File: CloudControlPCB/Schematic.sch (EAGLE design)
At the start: 29 parts, among them J1 AUDIO_JACK_TRRSSMD_RA, U1 LPC4088FBD208, U2 SGTL5000XNLA3R2, U3 LD1117S33CTR, X1 PHB_1MM27_2X05_SNT

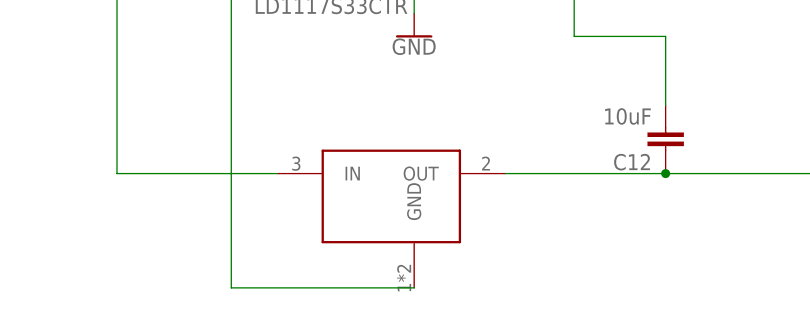
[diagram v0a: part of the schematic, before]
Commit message: Fixed 1.8V regulator connections
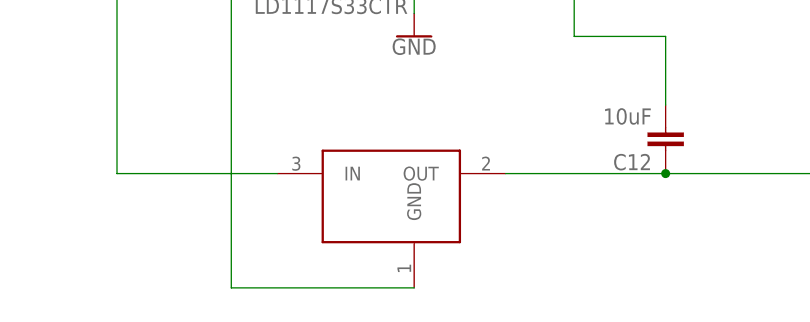
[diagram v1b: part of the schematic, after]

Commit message: finished routing
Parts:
- added C15: 0.1uF, SparkFun-Capacitors:0.1UF-0603-25V-(+80/-20%)
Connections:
- net GND: now also C15.2
- net VCC: now also C15.1
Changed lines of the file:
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@@
 <part name="U3" library="LD1117S33CTR" deviceset="LD1117S33CTR" device=""/>
 <part name="U$1" library="SOT230P700X180-4N" deviceset="SOT230P700X180-4N" device=""/>
+<part name="C15" library="SparkFun-Capacitors" deviceset="0.1UF" device="-0603-25V-(+80/-20%)" value="0.1uF"/>
 </parts>
 <sheets>
@@
 </instance>
 <instance part="U$1" gate="G$1" x="-104.14" y="-101.6" smashed="yes"/>
+<instance part="C15" gate="G$1" x="-116.84" y="-104.14" smashed="yes">
+<attribute name="NAME" x="-115.316" y="-101.219" size="1.778" layer="95" font="vector"/>
+<attribute name="VALUE" x="-115.316" y="-106.299" size="1.778" layer="96" font="vector"/>
+</instance>
 </instances>
 <busses>
@@
 <wire x1="-127" y1="-71.12" x2="-127" y2="-76.2" width="0.1524" layer="91"/>
 <junction x="-127" y="-76.2"/>
-<wire x1="-101.6" y1="-109.22" x2="-121.92" y2="-109.22" width="0.1524" layer="91"/>
+<wire x1="-101.6" y1="-109.22" x2="-116.84" y2="-109.22" width="0.1524" layer="91"/>
+<wire x1="-116.84" y1="-109.22" x2="-121.92" y2="-109.22" width="0.1524" layer="91"/>
 <wire x1="-121.92" y1="-109.22" x2="-121.92" y2="-76.2" width="0.1524" layer="91"/>
 <junction x="-121.92" y="-76.2"/>
@@
 <wire x1="-101.6" y1="-71.12" x2="-101.6" y2="-76.2" width="0.1524" layer="91"/>
 <pinref part="U$1" gate="G$1" pin="GND"/>
+<pinref part="C15" gate="G$1" pin="2"/>
+<wire x1="-116.84" y1="-106.68" x2="-116.84" y2="-109.22" width="0.1524" layer="91"/>
+<junction x="-116.84" y="-109.22"/>
 </segment>
 <segment>
@@
 <junction x="-127" y="-60.96"/>
 <pinref part="U$1" gate="G$1" pin="IN"/>
-</segment>
-</net>
+<pinref part="C15" gate="G$1" pin="1"/>
+<wire x1="-116.84" y1="-96.52" x2="-116.84" y2="-99.06" width="0.1524" layer="91"/>
+<junction x="-116.84" y="-96.52"/>
+</segment>
+</net>
